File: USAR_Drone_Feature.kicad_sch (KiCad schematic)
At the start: 48 parts, among them J1 DB128L-5.08-2P-BK-S, J2 DB128L-5.08-2P-BK-S, J3 Conn_02x04_Odd_Even, J4 Conn_01x04_Socket, J5 Conn_01x04_Socket, J6 Conn_01x04_Socket, SW1 TS-1088-AR02016, SW2 TS-1088-AR02016, U1 ESP32-S3-WROOM-1(N16R8)

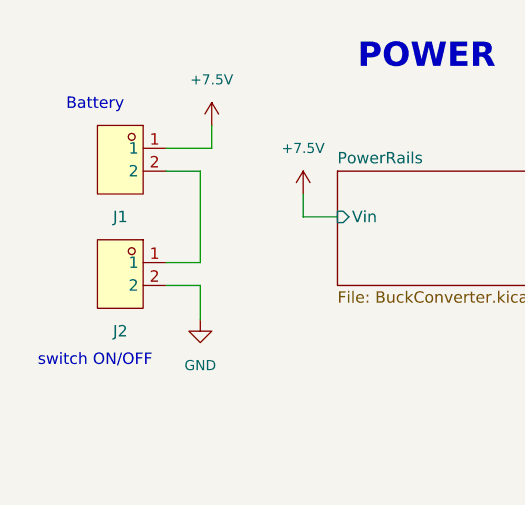
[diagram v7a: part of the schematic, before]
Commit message: ajuste de footprints, reposicionamiento de agujeros
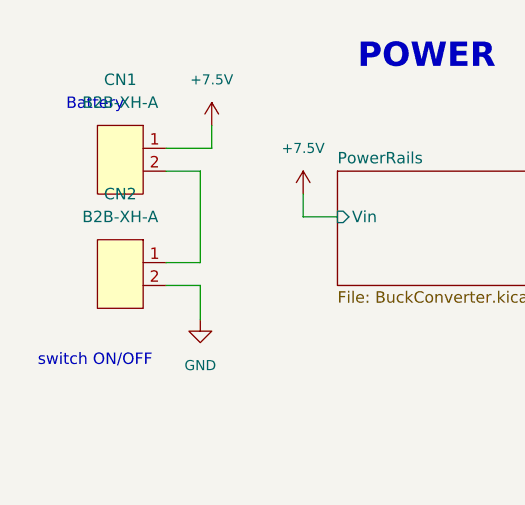
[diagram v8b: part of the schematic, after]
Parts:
- removed J1, J2: DB128L-5.08-2P-BK-S, EasyEDA:CONN-TH_2P-P5.08_DB128L-5.08-2P-BK-S, symbol EasyEDA:DB128L-5.08-2P-BK-S
- added CN1, CN2: B2B-XH-A, EasyEDA:CONN-TH_B2B-XH-A-LF-SN, symbol EasyEDA:B2B-XH-A
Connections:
- net +7.5V: now also CN1.1
- net GND: now also CN2.2
- new net: CN1.2, CN2.1
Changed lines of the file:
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@@
 	)
 	(symbol
+		(lib_id "EasyEDA:B2B-XH-A")
+		(at 26.67 45.72 0)
+		(mirror y)
+		(unit 1)
+		(body_style 1)
+		(exclude_from_sim no)
+		(in_bom yes)
+		(on_board yes)
+		(in_pos_files yes)
+		(dnp no)
+		(fields_autoplaced yes)
+		(property "Reference" "CN2"
+			(at 27.94 36.83 0)
+			(show_name no)
+			(do_not_autoplace no)
+			(effects
+				(font
+					(size 1.27 1.27)
+				)
+			)
+		)
+		(property "Value" "B2B-XH-A"
+			(at 27.94 39.37 0)
+			(show_name no)
+			(do_not_autoplace no)
+			(effects
+				(font
+					(size 1.27 1.27)
+				)
+			)
+		)
+		(property "Footprint" "EasyEDA:CONN-TH_B2B-XH-A-LF-SN"
+			(at 26.67 54.61 0)
+			(hide yes)
+			(show_name no)
+			(do_not_autoplace no)
+			(effects
+				(font
+					(size 1.27 1.27)
+				)
+			)
+		)
+		(property "Datasheet" "https://lcsc.com/product-detail/XH-Connectors_JST_B2B-XH-A-LF-SN_XHsocket-1-2P-pitch2-5mm_C158012.html"
+			(at 26.67 57.15 0)
+			(hide yes)
+			(show_name no)
+			(do_not_autoplace no)
+			(effects
+				(font
+					(size 1.27 1.27)
+				)
+			)
+		)
+		(property "Description" ""
+			(at 26.67 45.72 0)
+			(hide yes)
+			(show_name no)
+			(do_not_autoplace no)
+			(effects
+				(font
+					(size 1.27 1.27)
+				)
+			)
+		)
+		(property "Manufacturer" "JST"
+			(at 26.67 59.69 0)
+			(hide yes)
+			(show_name no)
+			(do_not_autoplace no)
+			(effects
+				(font
+					(size 1.27 1.27)
+				)
+			)
+		)
+		(property "MPN" "B2B-XH-A(LF)(SN)"
+			(at 26.67 62.23 0)
+			(hide yes)
+			(show_name no)
+			(do_not_autoplace no)
+			(effects
+				(font
+					(size 1.27 1.27)
+				)
+			)
+		)
+		(property "LCSC Part" "C158012"
+			(at 26.67 64.77 0)
+			(hide yes)
+			(show_name no)
+			(do_not_autoplace no)
+			(effects
+				(font
+					(size 1.27 1.27)
+				)
+			)
+		)
+		(pin "1"
+		)
+		(pin "2"
+		)
+		(instances
+			(project "USAR_Drone_Feature"
+				(path "/b3437995-bb94-4c2f-9ed8-b1af477fe956"
+					(reference "CN2")
+					(unit 1)
+				)
+			)
+		)
+	)
+	(symbol
 		(lib_id "Connector:Conn_01x04_Socket")
 		(at 373.38 160.02 0)
@@
 	)
 	(symbol
-		(lib_id "EasyEDA:DB128L-5.08-2P-BK-S")
-		(at 33.02 29.21 0)
-		(mirror y)
-		(unit 1)
-		(body_style 1)
-		(exclude_from_sim no)
-		(in_bom yes)
-		(on_board yes)
-		(in_pos_files yes)
-		(dnp no)
-		(property "Reference" "J1"
-			(at 27.94 39.37 0)
-			(show_name no)
-			(do_not_autoplace no)
-			(effects
-				(font
-					(size 1.27 1.27)
-				)
-			)
-		)
-		(property "Value" "DB128L-5.08-2P-BK-S"
-			(at 24.13 34.2899 0)
-			(hide yes)
-			(show_name no)
-			(do_not_autoplace no)
-			(effects
-				(font
-					(size 1.12 1.12)
-				)
-				(justify left)
-			)
-		)
-		(property "Footprint" "EasyEDA:CONN-TH_2P-P5.08_DB128L-5.08-2P-BK-S"
-			(at 33.02 41.91 0)
-			(hide yes)
-			(show_name no)
-			(do_not_autoplace no)
-			(effects
-				(font
-					(size 1.27 1.27)
-				)
-			)
-		)
-		(property "Datasheet" "https://lcsc.com/product-detail/Screw-terminal_DIBO-DB128L-5-08-2P-BK-S_C430601.html"
-			(at 33.02 44.45 0)
-			(hide yes)
-			(show_name no)
-			(do_not_autoplace no)
-			(effects
-				(font
-					(size 1.27 1.27)
-				)
-			)
-		)
-		(property "Description" "CONECTOR 24V"
-			(at 33.02 29.21 0)
-			(hide yes)
-			(show_name no)
-			(do_not_autoplace no)
-			(effects
-				(font
-					(size 1.27 1.27)
-				)
-			)
-		)
-		(property "LCSC Part" "C430601"
-			(at 33.02 46.99 0)
-			(hide yes)
-			(show_name no)
-			(do_not_autoplace no)
-			(effects
-				(font
-					(size 1.27 1.27)
-				)
-			)
-		)
-		(pin "2"
-		)
-		(pin "1"
-		)
-		(instances
-			(project "USAR_Drone_Feature"
-				(path "/b3437995-bb94-4c2f-9ed8-b1af477fe956"
-					(reference "J1")
-					(unit 1)
-				)
-			)
-		)
-	)
-	(symbol
 		(lib_id "power:+7.5V")
 		(at 38.1 29.21 0)
@@
 	)
 	(symbol
-		(lib_id "EasyEDA:DB128L-5.08-2P-BK-S")
-		(at 33.02 41.91 0)
-		(mirror y)
+		(lib_id "EasyEDA:TS-1088-AR02016")
+		(at 334.01 49.53 0)
 		(unit 1)
 		(body_style 1)
@@
 		(in_pos_files yes)
 		(dnp no)
-		(property "Reference" "J2"
-			(at 27.94 52.07 0)
+		(fields_autoplaced yes)
+		(property "Reference" "SW2"
+			(at 334.01 44.45 0)
 			(show_name no)
 			(do_not_autoplace no)
@@
 			)
 		)
-		(property "Value" "DB128L-5.08-2P-BK-S"
-			(at 24.13 46.9899 0)
+		(property "Value" "TS-1088-AR02016"
+			(at 334.01 46.99 0)
 			(hide yes)
 			(show_name no)
@@
 					(size 1.12 1.12)
 				)
-				(justify left)
 			)
 		)
-		(property "Footprint" "EasyEDA:CONN-TH_2P-P5.08_DB128L-5.08-2P-BK-S"
-			(at 33.02 54.61 0)
+		(property "Footprint" "EasyEDA:SW-SMD_L3.9-W3.0-P4.45"
+			(at 334.01 58.42 0)
+			(hide yes)
+			(show_name no)
+			(do_not_autoplace no)
+			(effects
+				(font
+					(size 1.27 1.27)
+				)
+			)
+		)
+		(property "Datasheet" "https://lcsc.com/product-detail/Tactile-Switches_XUNPU-TS-1088-AR02016_C720477.html"
+			(at 334.01 60.96 0)
 			(hide yes)
 			(show_name no)
@@
 			)
 		)
-		(property "Datasheet" "https://lcsc.com/product-detail/Screw-terminal_DIBO-DB128L-5-08-2P-BK-S_C430601.html"
-			(at 33.02 57.15 0)
+		(property "Description" ""
+			(at 334.01 49.53 0)
 			(hide yes)
 			(show_name no)
@@
 			)
 		)
-		(property "Description" "CONECTOR 24V"
-			(at 33.02 41.91 0)
+		(property "Manufacturer" "XUNPU(讯普)"
+			(at 334.01 63.5 0)
 			(hide yes)
 			(show_name no)
@@
 			)
 		)
-		(property "LCSC Part" "C430601"
-			(at 33.02 59.69 0)
+		(property "MPN" "TS-1088-AR02016"
+			(at 334.01 66.04 0)
+			(hide yes)
+			(show_name no)
+			(do_not_autoplace no)
+			(effects
+				(font
+					(size 1.27 1.27)
+				)
+			)
+		)
+		(property "LCSC Part" "C720477"
+			(at 334.01 68.58 0)
 			(hide yes)
 			(show_name no)
@@
 			(project "USAR_Drone_Feature"
 				(path "/b3437995-bb94-4c2f-9ed8-b1af477fe956"
-					(reference "J2")
+					(reference "SW2")
 					(unit 1)
 				)
@@
 	)
 	(symbol
-		(lib_id "EasyEDA:TS-1088-AR02016")
-		(at 334.01 49.53 0)
+		(lib_id "EasyEDA:B2B-XH-A")
+		(at 26.67 33.02 0)
+		(mirror y)
 		(unit 1)
 		(body_style 1)
@@
 		(dnp no)
 		(fields_autoplaced yes)
-		(property "Reference" "SW2"
-			(at 334.01 44.45 0)
+		(property "Reference" "CN1"
+			(at 27.94 24.13 0)
 			(show_name no)
 			(do_not_autoplace no)
@@
 			)
 		)
-		(property "Value" "TS-1088-AR02016"
-			(at 334.01 46.99 0)
-			(hide yes)
+		(property "Value" "B2B-XH-A"
+			(at 27.94 26.67 0)
 			(show_name no)
 			(do_not_autoplace no)
 			(effects
 				(font
-					(size 1.12 1.12)
+					(size 1.27 1.27)
 				)
 			)
 		)
-		(property "Footprint" "EasyEDA:SW-SMD_L3.9-W3.0-P4.45"
-			(at 334.01 58.42 0)
+		(property "Footprint" "EasyEDA:CONN-TH_B2B-XH-A-LF-SN"
+			(at 26.67 41.91 0)
 			(hide yes)
 			(show_name no)
@@
 			)
 		)
-		(property "Datasheet" "https://lcsc.com/product-detail/Tactile-Switches_XUNPU-TS-1088-AR02016_C720477.html"
-			(at 334.01 60.96 0)
+		(property "Datasheet" "https://lcsc.com/product-detail/XH-Connectors_JST_B2B-XH-A-LF-SN_XHsocket-1-2P-pitch2-5mm_C158012.html"
+			(at 26.67 44.45 0)
 			(hide yes)
 			(show_name no)
@@
 		)
 		(property "Description" ""
-			(at 334.01 49.53 0)
+			(at 26.67 33.02 0)
 			(hide yes)
 			(show_name no)
@@
 			)
 		)
-		(property "Manufacturer" "XUNPU(讯普)"
-			(at 334.01 63.5 0)
+		(property "Manufacturer" "JST"
+			(at 26.67 46.99 0)
 			(hide yes)
 			(show_name no)
@@
 			)
 		)
-		(property "MPN" "TS-1088-AR02016"
-			(at 334.01 66.04 0)
+		(property "MPN" "B2B-XH-A(LF)(SN)"
+			(at 26.67 49.53 0)
 			(hide yes)
 			(show_name no)
@@
 			)
 		)
-		(property "LCSC Part" "C720477"
-			(at 334.01 68.58 0)
+		(property "LCSC Part" "C158012"
+			(at 26.67 52.07 0)
 			(hide yes)
 			(show_name no)
@@
 			)
 		)
-		(pin "2"
-		)
 		(pin "1"
 		)
+		(pin "2"
+		)
 		(instances
 			(project "USAR_Drone_Feature"
 				(path "/b3437995-bb94-4c2f-9ed8-b1af477fe956"
-					(reference "SW2")
+					(reference "CN1")
 					(unit 1)
 				)
